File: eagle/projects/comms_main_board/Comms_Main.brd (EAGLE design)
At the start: 101.6 x 95.2 mm, 190 parts, among them J1 WRL-00593, J10 MOL-SL-2-RA, J11 MOL-SL-3-RA, J12 MOL-SL-3-RA, J13 MOL-SL-3-RA, J14 MOL-SL-3-RA, J15 MOL-SL-2-RA, J16 MOL-MINIJR-2P-RA, J17 MOL-MINIJR-2P-RA, J18 MOL-MINIJR-2P-RA, J19 MOL-MINIJR-2P-RA, J2 PRT-12639, J20 MOL-SL-2-RA, J21 RECEPTACLE-2x2-254MM, J22 MOL-SL-2-RA, J3 PRT-12639, J4 PRT-12639, J5 PRT-12639, J6 MOL-SL-3-RA, J7 MOL-SL-5-RA, J8 RECEPTACLE-2x20-254MM, J9 MOL-SL-3-RA, Q1 CSD17579Q3A, U1 TPS562209DDCT, U10 MCP4541-103E/MS, U11 TPS562209DDCT, U12 MMBT3904-HF, U13 MAX3232CSE+, U14 MAX4311, U15 MAX6371, U2 LP2985-33DBVR, U3 LP5900TLX-3.3/NOPB, U4 TPS562209DDCT, U6 LM3488MMX/NOPB, U7 PCT2075D,118, U8 MS560702BA03-50, U9 MAX-M8Q

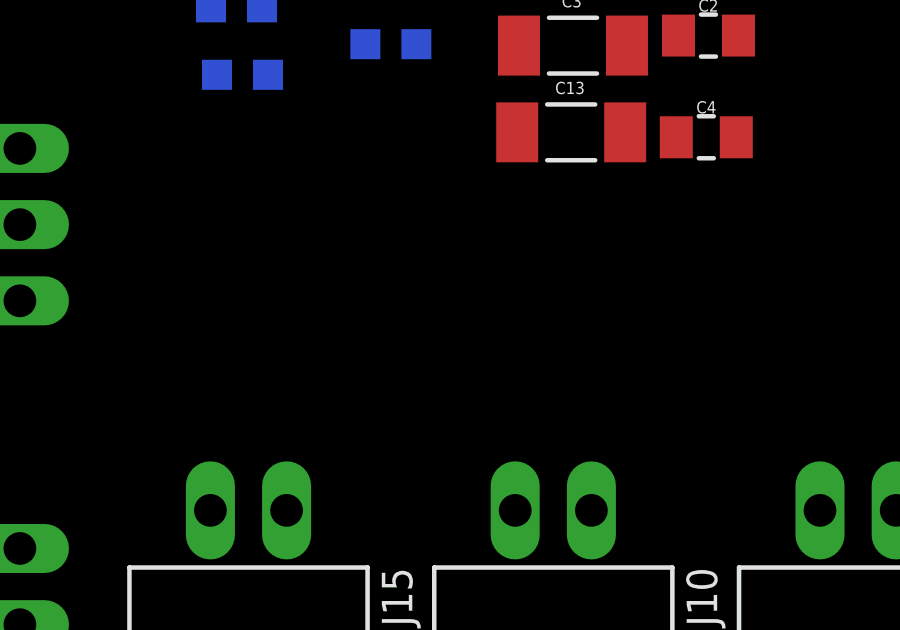
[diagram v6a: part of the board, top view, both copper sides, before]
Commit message: Added OSD power control circuit
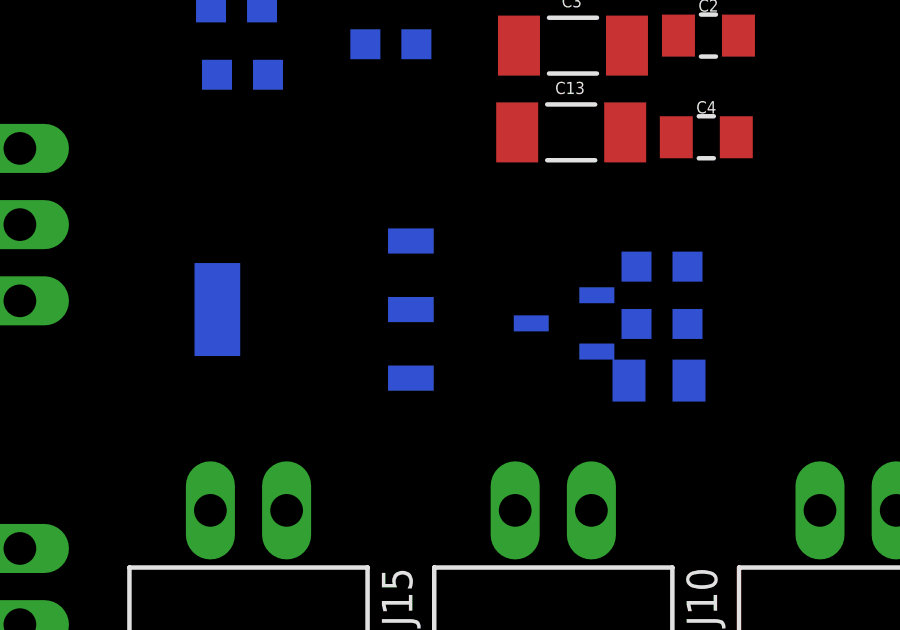
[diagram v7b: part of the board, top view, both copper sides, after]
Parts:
- added R10: 0.0, comms:R0805
- added R7, R8: 10k, comms:R0603
- added U16: 2N7002P,215, comms:SOT95P230X110-3N
- added U5: NDT2955, comms:SOT230P700X180-4N
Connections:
- removed net PI_GPIO5: J8.29, TP21.TP
- new net 12V_PI_CONTROLLED: J20.1, R10.1, U5.2, U5.3
- new net 12V_PMOS_G: R8.1, U16.3, U5.1
- new net PI_12V_CONTROL: J8.29, R7.1, TP21.TP, U16.1
- net 12V_BOARD: now also R10.2, R8.2, U5.4; no longer J20.1
- net 3P3V_RS232: now also R7.2
- net GND: now also U16.2

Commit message: Continued part placement
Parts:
- moved L3 80.6 mm to (45.8, 41.3)
- moved L1 76.2 mm to (34.2, 33.7)
- moved L4 66.6 mm to (61.0, 45.0)
- moved L2 59.5 mm to (56.7, 29.1)
- moved R6 41.9 mm to (43.1, 48.0)
- moved L6 41.0 mm to (81.2, 38.9)
- moved R5 39.2 mm to (47.3, 60.1)
- moved SH1 39.2 mm to (50.7, 60.2)
- moved R11 36.4 mm to (47.1, 58.1)
- moved C20 33.6 mm to (57.9, 55.4)
- moved C12 33.4 mm to (63.0, 28.8)
- moved C18 32.1 mm to (47.5, 49.9)
- moved U3 31.2 mm to (80.4, 53.9)
- moved Q1 30.2 mm to (53.0, 55.4)
- moved C24 27.5 mm to (80.2, 29.9)
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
